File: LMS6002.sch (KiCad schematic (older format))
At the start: 43 parts, among them U3 LMS6002DR2

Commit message: Schematic is done except RF.
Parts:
- removed C27, C30, C31, C32, C33, C35, C36, C39, C40, C44, C46, C47, C48, C50, C51, C52, C53, C55: 100n, Capacitors_SMD:C_0603_HandSoldering, symbol C
- removed C28, C29, C37: 1u, Capacitors_SMD:C_0603_HandSoldering, symbol C
- removed C34, C38, C54: 33p, Capacitors_SMD:C_0603_HandSoldering, symbol C
- removed L2, L3: Ferrite_Bead, Inductors_SMD:L_0603_HandSoldering, symbol Ferrite_Bead
- removed R8, R9: 22, Resistors_SMD:R_0603_HandSoldering, symbol R
- removed unit 1 of U3
- added unit 2 of U3
- C41, C42, C43, C45, C49, C56, C57: footprint Capacitors_SMD:C_0603_HandSoldering -> Capacitors_SMD:C_0402
- R10, R12, R13, R14, R15: footprint Resistors_SMD:R_0603_HandSoldering -> Resistors_SMD:R_0402
- R11: value 1k2 -> 1.2k; footprint Resistors_SMD:R_0603_HandSoldering -> Resistors_SMD:R_0402
- R16: value 6k8 -> 6.8k; footprint Resistors_SMD:R_0603_HandSoldering -> Resistors_SMD:R_0402
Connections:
- net labels added: CLK0, LMS_MISO, LMS_MOSI, LMS_RESET, LMS_RX_CLK, LMS_RX_EN, LMS_RX_IQSEL, LMS_SCLK, LMS_TX_CLK, LMS_TX_EN, LMS_TX_IQSEL, RXD0, RXD1, RXD10, RXD11, RXD2, RXD3, RXD4, RXD5, RXD6, RXD7, RXD8, RXD9, RXD[0..11], TXD0, TXD1, TXD10, TXD11, TXD2, TXD3, TXD4, TXD5, TXD6, TXD7, TXD8, TXD9, TXD[0..11], ~LMS_CS
- net labels removed: LMS_A1V8, LMS_A3V3, LMS_D1V8, LMS_D3V3, LMS_IO
- wire segments 81 -> 64
- no-connect marks 10 -> 13
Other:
- moved on the sheet: C41, C42, C43, C45, C49, C56, C57, R10, R11, R12, R13, R14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

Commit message: Placed most components for FTDI. Begin tracing FT601
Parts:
- C41, C42, C43, C45, C49, C56, C57: footprint Capacitors_SMD:C_0402 -> Capacitors_SMD:C_0603
- R10, R11, R12, R13, R14, R15, R16: footprint Resistors_SMD:R_0402 -> Resistors_SMD:R_0603
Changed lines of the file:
@@
 EESchema Schematic File Version 2
-LIBS:sdr-rescue
 LIBS:power
 LIBS:device
@@
 LIBS:sdr
 LIBS:usb-type-c
-LIBS:sdr-cache
 EELAYER 25 0
 EELAYER END
@@
 $EndComp
 $Comp
-L GNDD #PWR037
+L GNDD #PWR038
 U 1 1 58A337CD
 P 3200 7400
-F 0 "#PWR037" H 3200 7150 50  0001 C CNN
+F 0 "#PWR038" H 3200 7150 50  0001 C CNN
 F 1 "GNDD" H 3200 7250 50  0000 C CNN
 F 2 "" H 3200 7400 50  0000 C CNN
@@
 F 0 "C41" H 925 6400 50  0000 L CNN
 F 1 "470p" H 925 6200 50  0000 L CNN
-F 2 "Capacitors_SMD:C_0402" H 938 6150 50  0001 C CNN
+F 2 "Capacitors_SMD:C_0603" H 938 6150 50  0001 C CNN
 F 3 "" H 900 6300 50  0000 C CNN
 	1    900  6300
@@
 F 0 "C42" H 1375 6400 50  0000 L CNN
 F 1 "10n" H 1375 6200 50  0000 L CNN
-F 2 "Capacitors_SMD:C_0402" H 1388 6150 50  0001 C CNN
+F 2 "Capacitors_SMD:C_0603" H 1388 6150 50  0001 C CNN
 F 3 "" H 1350 6300 50  0000 C CNN
 	1    1350 6300
@@
 F 0 "C49" H 2275 6400 50  0000 L CNN
 F 1 "150p" H 2275 6200 50  0000 L CNN
-F 2 "Capacitors_SMD:C_0402" H 2288 6150 50  0001 C CNN
+F 2 "Capacitors_SMD:C_0603" H 2288 6150 50  0001 C CNN
 F 3 "" H 2250 6300 50  0000 C CNN
 	1    2250 6300
@@
 F 0 "R10" V 1430 6700 50  0000 C CNN
 F 1 "820" V 1350 6700 50  0000 C CNN
-F 2 "Resistors_SMD:R_0402" V 1280 6700 50  0001 C CNN
+F 2 "Resistors_SMD:R_0603" V 1280 6700 50  0001 C CNN
 F 3 "" H 1350 6700 50  0000 C CNN
 	1    1350 6700
@@
 F 0 "R11" V 1880 6150 50  0000 C CNN
 F 1 "1.2k" V 1800 6150 50  0000 C CNN
-F 2 "Resistors_SMD:R_0402" V 1730 6150 50  0001 C CNN
+F 2 "Resistors_SMD:R_0603" V 1730 6150 50  0001 C CNN
 F 3 "" H 1800 6150 50  0000 C CNN
 	1    1800 6150
@@
 NoConn ~ 3200 4500
 $Comp
-L GNDD #PWR038
+L GNDD #PWR039
 U 1 1 58A3826F
 P 1350 6900
-F 0 "#PWR038" H 1350 6650 50  0001 C CNN
+F 0 "#PWR039" H 1350 6650 50  0001 C CNN
 F 1 "GNDD" H 1350 6750 50  0000 C CNN
 F 2 "" H 1350 6900 50  0000 C CNN
@@
 F 0 "C43" H 1675 5450 50  0000 L CNN
 F 1 "470p" H 1675 5250 50  0000 L CNN
-F 2 "Capacitors_SMD:C_0402" H 1688 5200 50  0001 C CNN
+F 2 "Capacitors_SMD:C_0603" H 1688 5200 50  0001 C CNN
 F 3 "" H 1650 5350 50  0000 C CNN
 	1    1650 5350
@@
 F 0 "C45" H 2125 5450 50  0000 L CNN
 F 1 "10n" H 2125 5250 50  0000 L CNN
-F 2 "Capacitors_SMD:C_0402" H 2138 5200 50  0001 C CNN
+F 2 "Capacitors_SMD:C_0603" H 2138 5200 50  0001 C CNN
 F 3 "" H 2100 5350 50  0000 C CNN
 	1    2100 5350
@@
 F 0 "C56" H 3025 5450 50  0000 L CNN
 F 1 "150p" H 3025 5250 50  0000 L CNN
-F 2 "Capacitors_SMD:C_0402" H 3038 5200 50  0001 C CNN
+F 2 "Capacitors_SMD:C_0603" H 3038 5200 50  0001 C CNN
 F 3 "" H 3000 5350 50  0000 C CNN
 	1    3000 5350
@@
 F 0 "R12" V 2180 5750 50  0000 C CNN
 F 1 "820" V 2100 5750 50  0000 C CNN
-F 2 "Resistors_SMD:R_0402" V 2030 5750 50  0001 C CNN
+F 2 "Resistors_SMD:R_0603" V 2030 5750 50  0001 C CNN
 F 3 "" H 2100 5750 50  0000 C CNN
 	1    2100 5750
@@
 F 0 "R13" V 2630 5200 50  0000 C CNN
 F 1 "1k2" V 2550 5200 50  0000 C CNN
-F 2 "Resistors_SMD:R_0402" V 2480 5200 50  0001 C CNN
+F 2 "Resistors_SMD:R_0603" V 2480 5200 50  0001 C CNN
 F 3 "" H 2550 5200 50  0000 C CNN
 	1    2550 5200
@@
 $EndComp
 $Comp
-L GNDD #PWR039
+L GNDD #PWR040
 U 1 1 58A38F2B
 P 2100 5900
-F 0 "#PWR039" H 2100 5650 50  0001 C CNN
+F 0 "#PWR040" H 2100 5650 50  0001 C CNN
 F 1 "GNDD" H 2100 5750 50  0000 C CNN
 F 2 "" H 2100 5900 50  0000 C CNN
@@
 F 0 "R14" V 2730 6650 50  0000 C CNN
 F 1 "390" V 2650 6650 50  0000 C CNN
-F 2 "Resistors_SMD:R_0402" V 2580 6650 50  0001 C CNN
+F 2 "Resistors_SMD:R_0603" V 2580 6650 50  0001 C CNN
 F 3 "" H 2650 6650 50  0000 C CNN
 	1    2650 6650
@@
 F 0 "R16" V 3030 6450 50  0000 C CNN
 F 1 "6.8k" V 2950 6450 50  0000 C CNN
-F 2 "Resistors_SMD:R_0402" V 2880 6450 50  0001 C CNN
+F 2 "Resistors_SMD:R_0603" V 2880 6450 50  0001 C CNN
 F 3 "" H 2950 6450 50  0000 C CNN
 	1    2950 6450
@@
 F 0 "R15" V 3030 6350 50  0000 C CNN
 F 1 "12k" V 2950 6350 50  0000 C CNN
-F 2 "Resistors_SMD:R_0402" V 2880 6350 50  0001 C CNN
+F 2 "Resistors_SMD:R_0603" V 2880 6350 50  0001 C CNN
 F 3 "" H 2950 6350 50  0000 C CNN
 	1    2950 6350
@@
 F 0 "C57" H 3075 6800 50  0000 L CNN
 F 1 "100n" H 3075 6600 50  0000 L CNN
-F 2 "Capacitors_SMD:C_0402" H 3088 6550 50  0001 C CNN
+F 2 "Capacitors_SMD:C_0603" H 3088 6550 50  0001 C CNN
 F 3 "" H 3050 6700 50  0000 C CNN
 	1    3050 6700
@@
 $EndComp
 $Comp
-L GNDD #PWR040
+L GNDD #PWR041
 U 1 1 58A3A1AF
 P 2650 6950
-F 0 "#PWR040" H 2650 6700 50  0001 C CNN
+F 0 "#PWR041" H 2650 6700 50  0001 C CNN
 F 1 "GNDD" H 2650 6800 50  0000 C CNN
 F 2 "" H 2650 6950 50  0000 C CNN

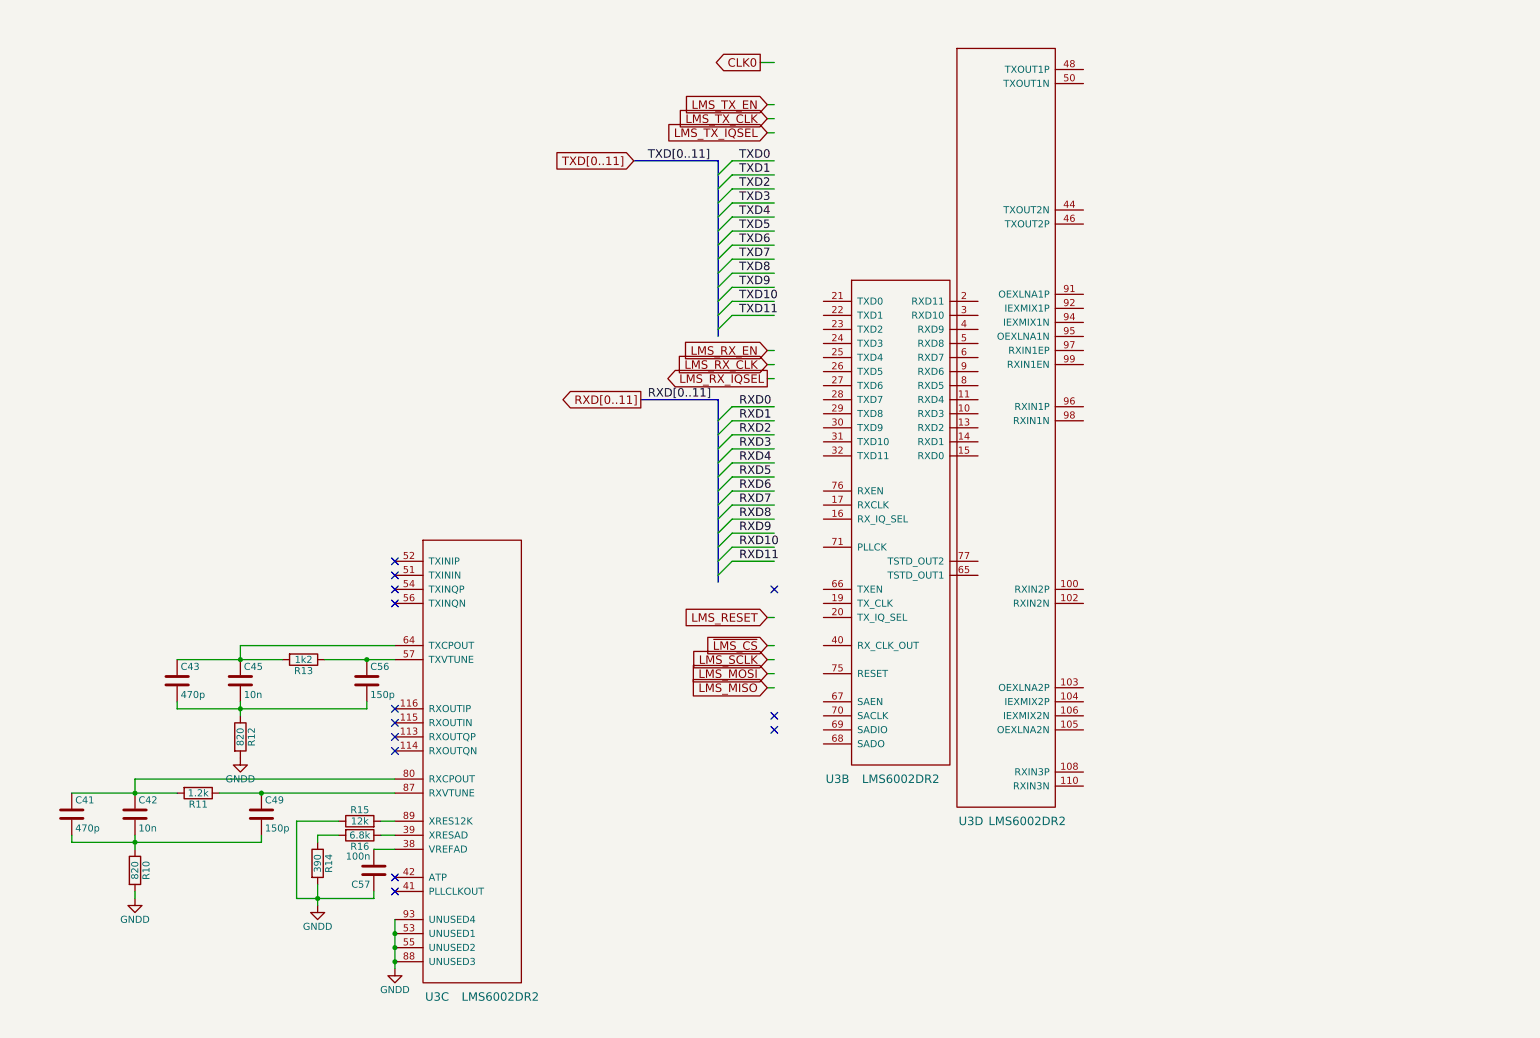
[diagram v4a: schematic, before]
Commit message: Start placing RF. Shield is ready. Fixed some net bugs.
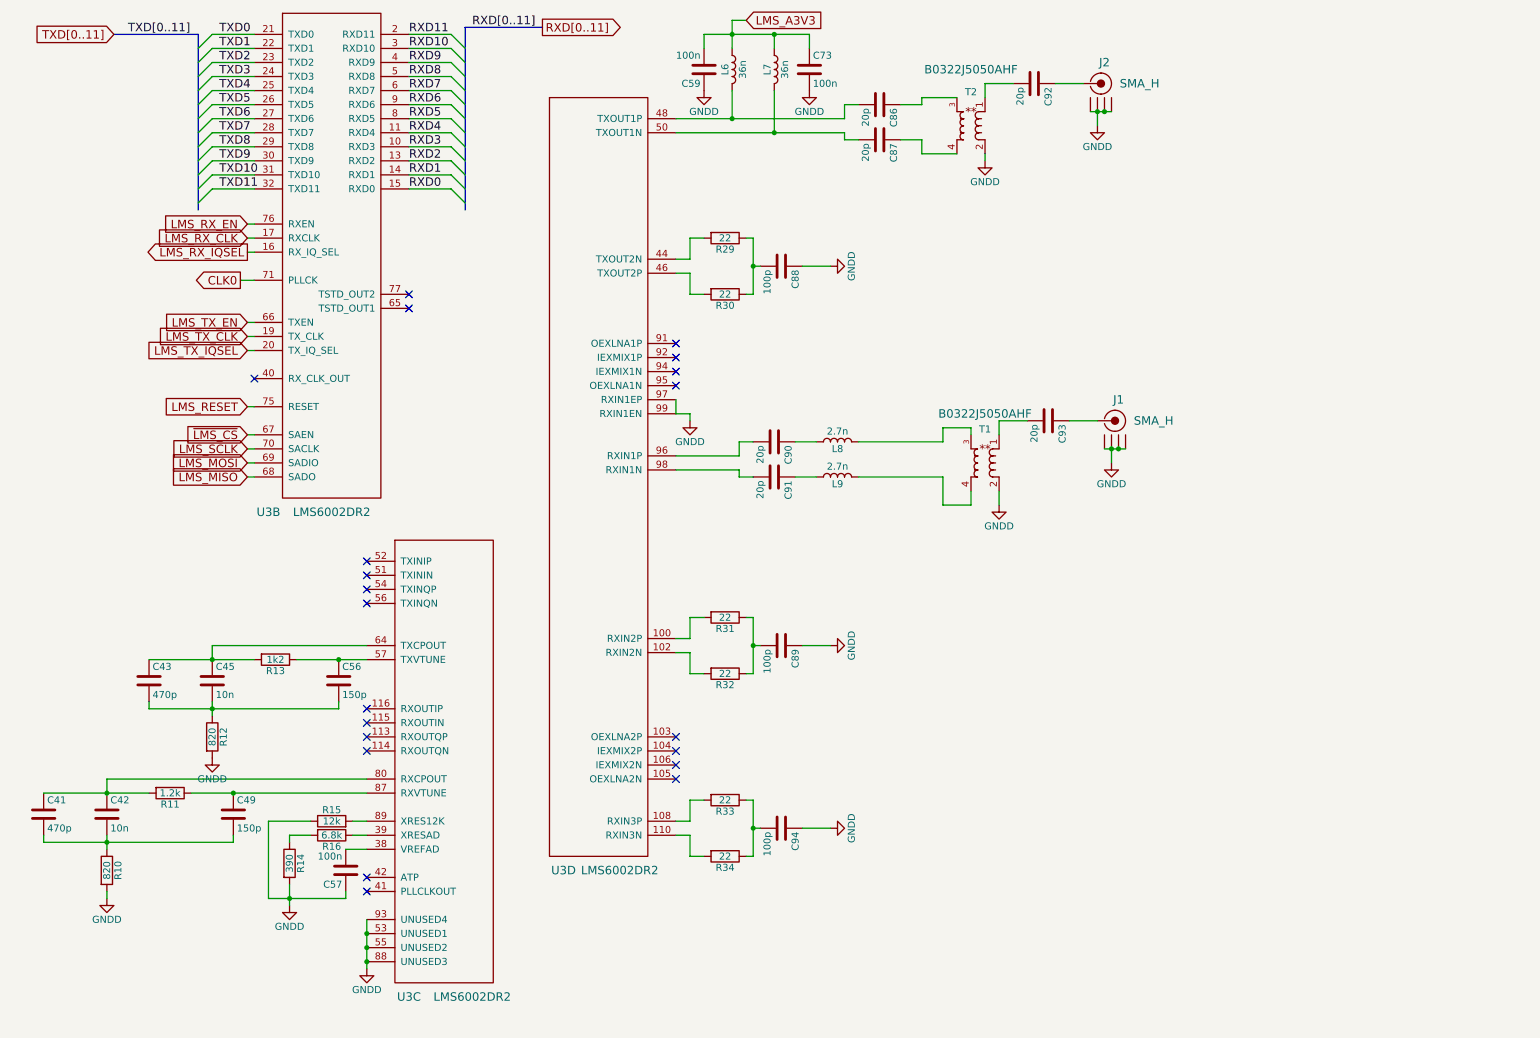
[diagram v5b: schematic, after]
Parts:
- added C59, C73: 100n, Capacitors_SMD:C_0603, symbol C
- added C86, C87, C90, C91, C92, C93: 20p, Capacitors_SMD:C_0603, symbol C
- added C88, C89, C94: 100p, Capacitors_SMD:C_0603, symbol C
- added J1, J2: SMA_H, sdr-foots:SMA_H, symbol SMA_H
- added L6, L7: 36n, Inductors_SMD:L_0603, symbol L
- added L8, L9: 2.7n, Inductors_SMD:L_0603, symbol L
- added R29, R30, R31, R32, R33, R34: 22, Resistors_SMD:R_0603, symbol R
- added T1, T2: B0322J5050, sdr-foots:B0322J5050, symbol B0322J5050
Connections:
- net labels added: LMS_A3V3
- wire segments 64 -> 148
- no-connect marks 13 -> 21
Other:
- moved on the sheet: C41, C42, C43, C45, C49, C56, C57, R10, R11, R12, R13, R14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

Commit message: Right before switching to full RPi
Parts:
- J1, J2: Manufacturer Emerson Network Power Connectivity Johnson -> RF Solutions; Manufacturer Part Number 142-0711-821 -> CON-SMA-EDGE-S
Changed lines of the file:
@@
 F 4 "Digi-Key" H 8250 4950 60  0001 C CNN "Vendor"
 F 5 "J629-ND" H 8250 5050 60  0001 C CNN "Vendor Part Number"
-F 6 "Emerson Network Power Connectivity Johnson" H 8250 4850 60  0001 C CNN "Manufacturer"
-F 7 "142-0711-821" H 8250 4750 60  0001 C CNN "Manufacturer Part Number"
+F 6 "RF Solutions" H 8250 4850 60  0001 C CNN "Manufacturer"
+F 7 "CON-SMA-EDGE-S" H 8250 4750 60  0001 C CNN "Manufacturer Part Number"
 F 8 "CONN, SMA, JACK, 50 OHM, EDGE MNT," H 8300 4600 60  0001 C CNN "Description"
 F 9 "SMA_H" H 8600 4100 60  0000 C CNN "Component Value"
@@
 F 4 "Digi-Key" H 8150 2550 60  0001 C CNN "Vendor"
 F 5 "J629-ND" H 8150 2650 60  0001 C CNN "Vendor Part Number"
-F 6 "Emerson Network Power Connectivity Johnson" H 8150 2450 60  0001 C CNN "Manufacturer"
-F 7 "142-0711-821" H 8150 2350 60  0001 C CNN "Manufacturer Part Number"
+F 6 "RF Solutions" H 8150 2450 60  0001 C CNN "Manufacturer"
+F 7 "CON-SMA-EDGE-S" H 8150 2350 60  0001 C CNN "Manufacturer Part Number"
 F 8 "CONN, SMA, JACK, 50 OHM, EDGE MNT," H 8200 2200 60  0001 C CNN "Description"
 F 9 "SMA_H" H 8500 1700 60  0000 C CNN "Component Value"
